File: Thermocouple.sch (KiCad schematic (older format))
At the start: 0 parts

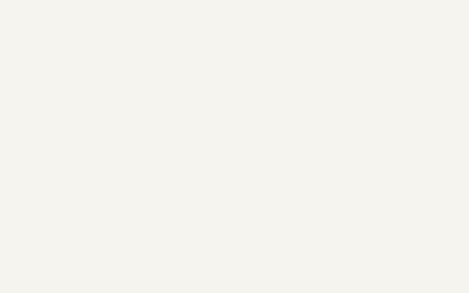
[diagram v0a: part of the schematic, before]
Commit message: Module Inputs & Outputs
Module Inputs and Outputs have been placed on the block diagram sheet
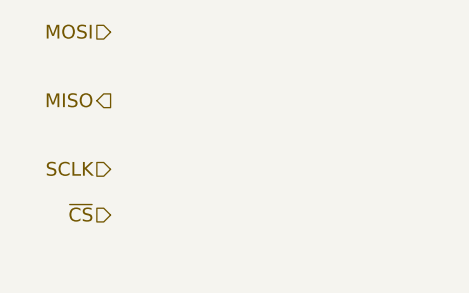
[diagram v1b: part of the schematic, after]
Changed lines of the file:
@@
 Text HLabel 7400 2600 2    60   Input ~ 0
 TC IN -
+Text HLabel 1300 1600 0    60   Input ~ 0
+MOSI
+Text HLabel 1300 1900 0    60   Output ~ 0
+MISO
+Text HLabel 1300 2200 0    60   Input ~ 0
+SCLK
+Text HLabel 1300 2400 0    60   Input ~ 0
+~CS
 $EndSCHEMATC

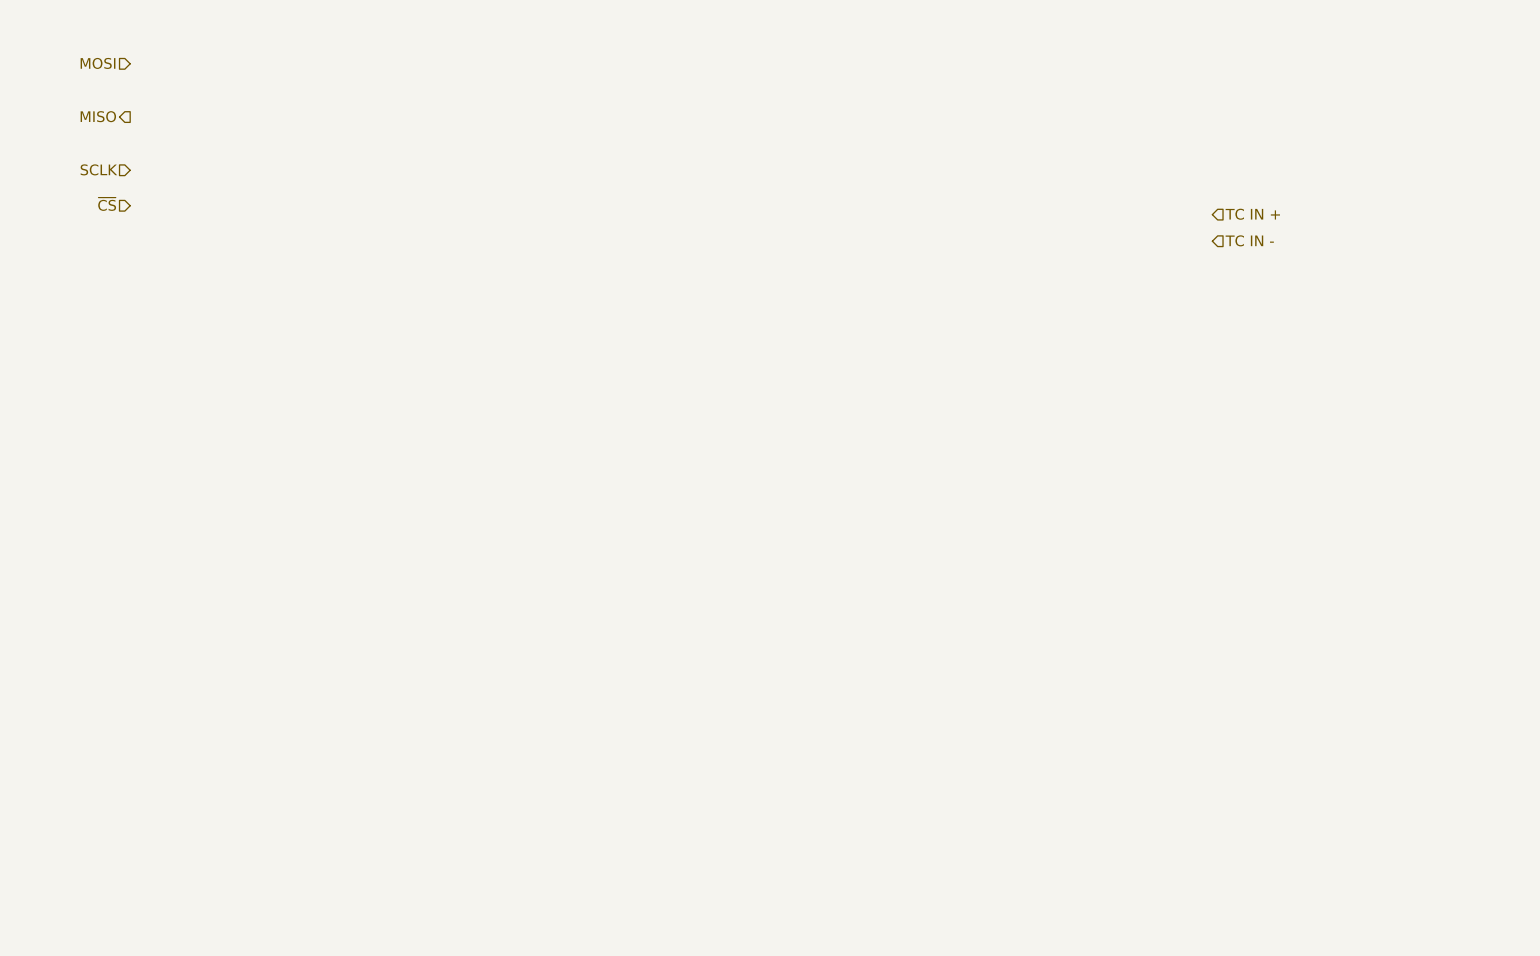
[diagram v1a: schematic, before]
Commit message: Thermocouple Generic Schematic
Added schematic pages for all modules and generic schematic for
Thermocouple instrumentation amp and sensor.
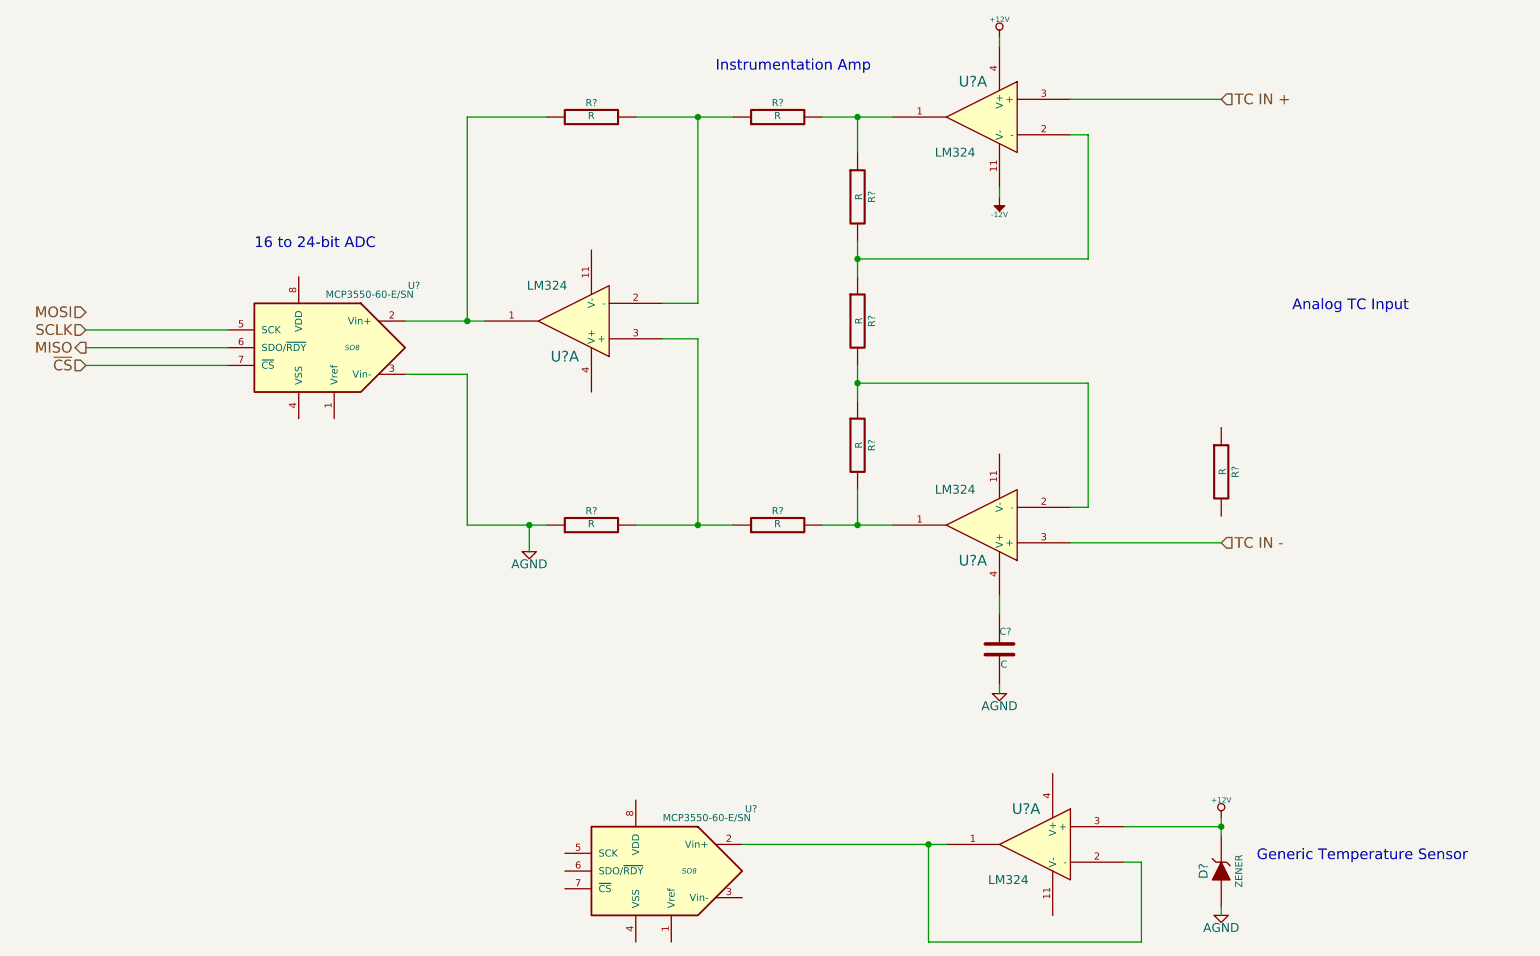
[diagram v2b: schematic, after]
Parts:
- added C?: C, ~, symbol C
- added D?: ZENER, ~, symbol ZENER
- added R? (x8): R, ~, symbol R
- added U? (x4): LM324, symbol LM324
- added U? (x2): MCP3550-60-E/SN, SO8, symbol MCP3550-60-E/SN
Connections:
- net MISO: now also U?.6 (SDO/~RDY~)
- net SCLK: now also U?.5 (SCK)
- net TC IN +: now also U?.3 (+)
- net TC IN -: now also U?.3 (+)
- net ~CS: now also U?.7 (~CS~)
- new net: R?.1, R?.2, U?.1
- new net: R?.1, R?.2, U?.2 (-) (x3)
- new net: R?.2, R?.2, U?.1
- new net: C?.1, U?.4 (V+)
- new net: R?.1, U?.1, U?.2 (Vin+)
- new net: R?.1, R?.2, U?.3 (+)
- new net: U?.1, U?.2 (-), U?.2 (Vin+)
- new net +12V: D?.2 (K), U?.3 (+), U?.4 (V+)
- new net -12V: U?.11 (V-)
- new net AGND: C?.2, D?.1 (A), R?.1, U?.3 (Vin-)
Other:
- note added: "16 to 24-bit ADC"
- note added: "Analog TC Input"
- note added: "Generic Temperature Sensor"
- note added: "Instrumentation Amp"
